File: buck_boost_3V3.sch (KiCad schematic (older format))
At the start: 10 parts

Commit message: Finally finished final draft
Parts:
- C13, C14, C17: renamed from C?; value 10 uF -> 10uF
- C15: renamed from C?; value 10 pF -> 10pF
- C16: renamed from C?; value 3.9 nF -> 3.9nF
- L2: renamed from L?; value 1.5 uH -> 1.5uH
- R4: renamed from R?; value 100 k -> 100k
- R5: renamed from R?; value 562 k -> 562k
- R6: renamed from R?; value 180 k -> 180k
- gave numbers to parts that had none: 1
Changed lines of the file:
@@
 $Descr A4 11693 8268
 encoding utf-8
-Sheet 5 6
+Sheet 4 6
 Title ""
 Date ""
@@
 AR Path="/60C6C1A9" Ref="IC?"  Part="1"
 AR Path="/60BA4931/60C6C1A9" Ref="IC?"  Part="1"
-AR Path="/60BA4931/60C66E04/60C6C1A9" Ref="IC?"  Part="1"
-F 0 "IC?" H 4900 4215 50  0000 C CNN
+AR Path="/60BA4931/60C66E04/60C6C1A9" Ref="IC2"  Part="1"
+F 0 "IC2" H 4900 4215 50  0000 C CNN
 F 1 "TPS63050YFFR" H 4900 4124 50  0000 C CNN
 F 2 "BGA12C40P3X4_129X169X62" H 4450 2900 50  0001 L CNN
@@
 AR Path="/60C6C1B2" Ref="L?"  Part="1"
 AR Path="/60BA4931/60C6C1B2" Ref="L?"  Part="1"
-AR Path="/60BA4931/60C66E04/60C6C1B2" Ref="L?"  Part="1"
-F 0 "L?" V 5090 2750 50  0000 C CNN
-F 1 "1.5 uH" V 4999 2750 50  0000 C CNN
+AR Path="/60BA4931/60C66E04/60C6C1B2" Ref="L2"  Part="1"
+F 0 "L2" V 5090 2750 50  0000 C CNN
+F 1 "1.5uH" V 4999 2750 50  0000 C CNN
 F 2 "" H 4900 2750 50  0001 C CNN
 F 3 "~" H 4900 2750 50  0001 C CNN
@@
 AR Path="/60C6C1C0" Ref="R?"  Part="1"
 AR Path="/60BA4931/60C6C1C0" Ref="R?"  Part="1"
-AR Path="/60BA4931/60C66E04/60C6C1C0" Ref="R?"  Part="1"
-F 0 "R?" H 6068 3596 50  0000 L CNN
-F 1 "562 k" H 6068 3505 50  0000 L CNN
+AR Path="/60BA4931/60C66E04/60C6C1C0" Ref="R5"  Part="1"
+F 0 "R5" H 6068 3596 50  0000 L CNN
+F 1 "562k" H 6068 3505 50  0000 L CNN
 F 2 "" V 6040 3540 50  0001 C CNN
 F 3 "~" H 6000 3550 50  0001 C CNN
@@
 AR Path="/60C6C1CA" Ref="R?"  Part="1"
 AR Path="/60BA4931/60C6C1CA" Ref="R?"  Part="1"
-AR Path="/60BA4931/60C66E04/60C6C1CA" Ref="R?"  Part="1"
-F 0 "R?" H 6068 3996 50  0000 L CNN
-F 1 "180 k" H 6068 3905 50  0000 L CNN
+AR Path="/60BA4931/60C66E04/60C6C1CA" Ref="R6"  Part="1"
+F 0 "R6" H 6068 3996 50  0000 L CNN
+F 1 "180k" H 6068 3905 50  0000 L CNN
 F 2 "" V 6040 3940 50  0001 C CNN
 F 3 "~" H 6000 3950 50  0001 C CNN
@@
 AR Path="/60C6C1DC" Ref="R?"  Part="1"
 AR Path="/60BA4931/60C6C1DC" Ref="R?"  Part="1"
-AR Path="/60BA4931/60C66E04/60C6C1DC" Ref="R?"  Part="1"
-F 0 "R?" H 6968 3846 50  0000 L CNN
-F 1 "100 k" H 6968 3755 50  0000 L CNN
+AR Path="/60BA4931/60C66E04/60C6C1DC" Ref="R4"  Part="1"
+F 0 "R4" H 6968 3846 50  0000 L CNN
+F 1 "100k" H 6968 3755 50  0000 L CNN
 F 2 "" V 6940 3790 50  0001 C CNN
 F 3 "~" H 6900 3800 50  0001 C CNN
@@
 AR Path="/60C6C1E8" Ref="C?"  Part="1"
 AR Path="/60BA4931/60C6C1E8" Ref="C?"  Part="1"
-AR Path="/60BA4931/60C66E04/60C6C1E8" Ref="C?"  Part="1"
-F 0 "C?" H 7415 4196 50  0000 L CNN
-F 1 "10 uF" H 7415 4105 50  0000 L CNN
+AR Path="/60BA4931/60C66E04/60C6C1E8" Ref="C14"  Part="1"
+F 0 "C14" H 7415 4196 50  0000 L CNN
+F 1 "10uF" H 7415 4105 50  0000 L CNN
 F 2 "" H 7338 4000 50  0001 C CNN
 F 3 "~" H 7300 4150 50  0001 C CNN
@@
 AR Path="/60C6C1F2" Ref="C?"  Part="1"
 AR Path="/60BA4931/60C6C1F2" Ref="C?"  Part="1"
-AR Path="/60BA4931/60C66E04/60C6C1F2" Ref="C?"  Part="1"
-F 0 "C?" H 7915 4196 50  0000 L CNN
-F 1 "10 uF" H 7915 4105 50  0000 L CNN
+AR Path="/60BA4931/60C66E04/60C6C1F2" Ref="C13"  Part="1"
+F 0 "C13" H 7915 4196 50  0000 L CNN
+F 1 "10uF" H 7915 4105 50  0000 L CNN
 F 2 "" H 7838 4000 50  0001 C CNN
 F 3 "~" H 7800 4150 50  0001 C CNN
@@
 AR Path="/60C6C210" Ref="C?"  Part="1"
 AR Path="/60BA4931/60C6C210" Ref="C?"  Part="1"
-AR Path="/60BA4931/60C66E04/60C6C210" Ref="C?"  Part="1"
-F 0 "C?" H 4215 4346 50  0000 L CNN
-F 1 "3.9 nF" H 4215 4255 50  0000 L CNN
+AR Path="/60BA4931/60C66E04/60C6C210" Ref="C16"  Part="1"
+F 0 "C16" H 4215 4346 50  0000 L CNN
+F 1 "3.9nF" H 4215 4255 50  0000 L CNN
 F 2 "" H 4138 4150 50  0001 C CNN
 F 3 "~" H 4100 4300 50  0001 C CNN
@@
 AR Path="/60C6C21A" Ref="C?"  Part="1"
 AR Path="/60BA4931/60C6C21A" Ref="C?"  Part="1"
-AR Path="/60BA4931/60C66E04/60C6C21A" Ref="C?"  Part="1"
-F 0 "C?" H 3715 3846 50  0000 L CNN
-F 1 "10 uF" H 3715 3755 50  0000 L CNN
+AR Path="/60BA4931/60C66E04/60C6C21A" Ref="C17"  Part="1"
+F 0 "C17" H 3715 3846 50  0000 L CNN
+F 1 "10uF" H 3715 3755 50  0000 L CNN
 F 2 "" H 3638 3650 50  0001 C CNN
 F 3 "~" H 3600 3800 50  0001 C CNN
@@
 AR Path="/60C6C22B" Ref="C?"  Part="1"
 AR Path="/60BA4931/60C6C22B" Ref="C?"  Part="1"
-AR Path="/60BA4931/60C66E04/60C6C22B" Ref="C?"  Part="1"
-F 0 "C?" H 6615 3996 50  0000 L CNN
-F 1 "10 pF" H 6615 3905 50  0000 L CNN
+AR Path="/60BA4931/60C66E04/60C6C22B" Ref="C15"  Part="1"
+F 0 "C15" H 6615 3996 50  0000 L CNN
+F 1 "10pF" H 6615 3905 50  0000 L CNN
 F 2 "" H 6538 3800 50  0001 C CNN
 F 3 "~" H 6500 3950 50  0001 C CNN

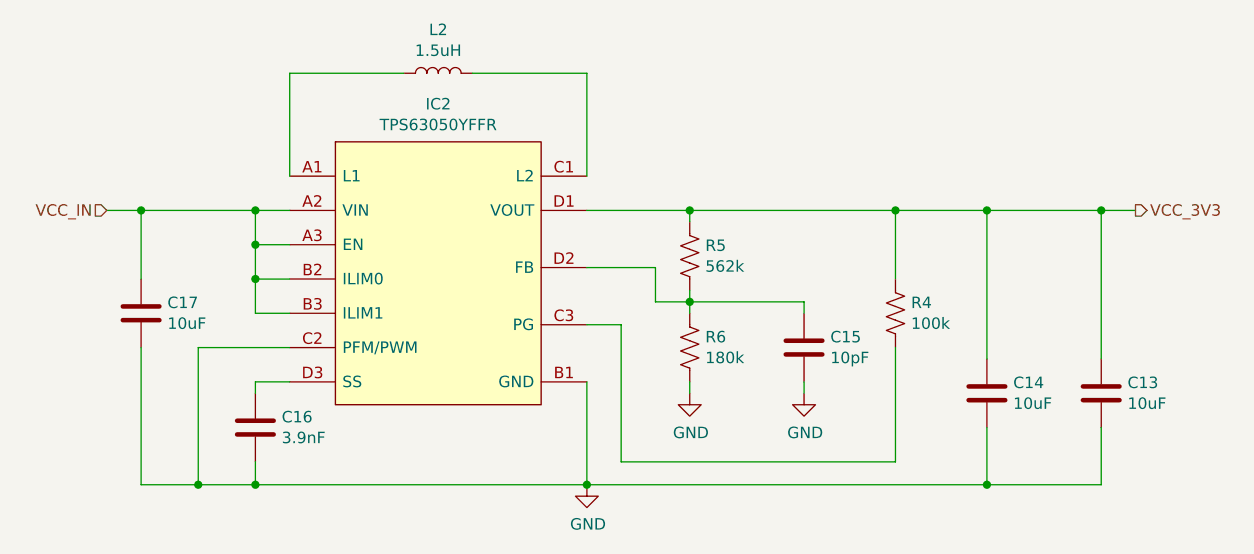
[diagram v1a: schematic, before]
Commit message: Fixed some symbols, assigned some footprints, and made wire labels
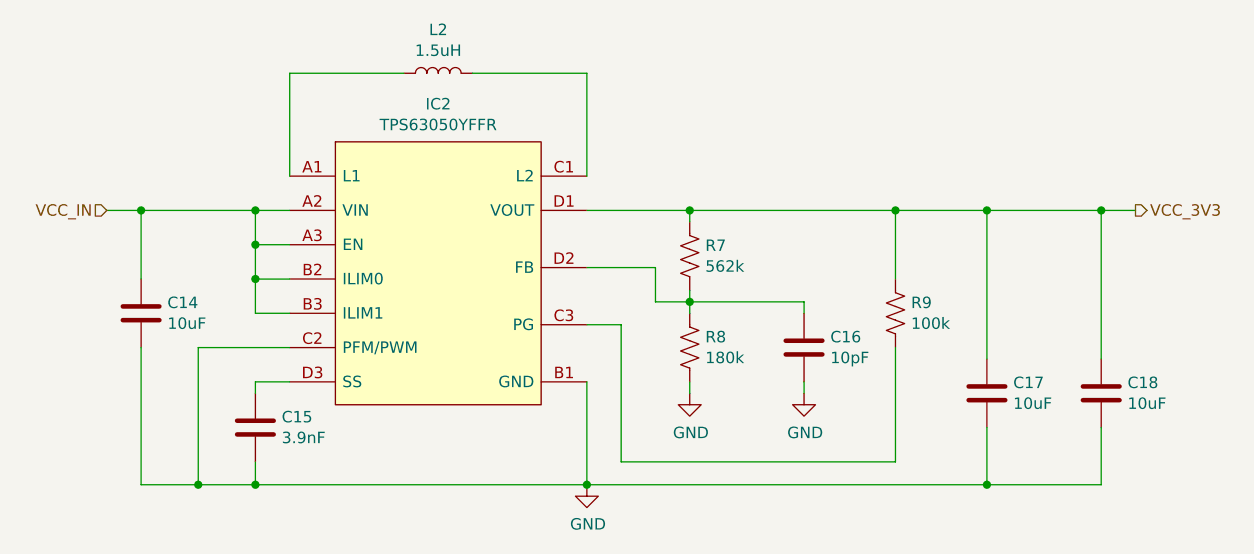
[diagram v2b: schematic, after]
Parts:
- IC2: footprint BGA12C40P3X4_129X169X62 -> Buck_Boost_IC:BGA12C40P3X4_129X169X62
- renumbered C17 to C14, C16 to C15, C15 to C16, C14 to C17, C13 to C18, R5 to R7, R6 to R8, R4 to R9
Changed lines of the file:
@@
 F 0 "IC2" H 4900 4215 50  0000 C CNN
 F 1 "TPS63050YFFR" H 4900 4124 50  0000 C CNN
-F 2 "BGA12C40P3X4_129X169X62" H 4450 2900 50  0001 L CNN
+F 2 "Buck_Boost_IC:BGA12C40P3X4_129X169X62" H 4450 2900 50  0001 L CNN
 F 3 "http://www.ti.com/lit/ds/symlink/tps63050.pdf" H 4450 2800 50  0001 L CNN
 F 4 "TPS6305x Single Inductor Buck-Boost with 1-A Switches and Adjustable Soft Start" H 4450 2700 50  0001 L CNN "Description"
@@
 AR Path="/60C6C1C0" Ref="R?"  Part="1"
 AR Path="/60BA4931/60C6C1C0" Ref="R?"  Part="1"
-AR Path="/60BA4931/60C66E04/60C6C1C0" Ref="R5"  Part="1"
-F 0 "R5" H 6068 3596 50  0000 L CNN
+AR Path="/60BA4931/60C66E04/60C6C1C0" Ref="R7"  Part="1"
+F 0 "R7" H 6068 3596 50  0000 L CNN
 F 1 "562k" H 6068 3505 50  0000 L CNN
 F 2 "" V 6040 3540 50  0001 C CNN
@@
 AR Path="/60C6C1CA" Ref="R?"  Part="1"
 AR Path="/60BA4931/60C6C1CA" Ref="R?"  Part="1"
-AR Path="/60BA4931/60C66E04/60C6C1CA" Ref="R6"  Part="1"
-F 0 "R6" H 6068 3996 50  0000 L CNN
+AR Path="/60BA4931/60C66E04/60C6C1CA" Ref="R8"  Part="1"
+F 0 "R8" H 6068 3996 50  0000 L CNN
 F 1 "180k" H 6068 3905 50  0000 L CNN
 F 2 "" V 6040 3940 50  0001 C CNN
@@
 AR Path="/60C6C1D1" Ref="#PWR?"  Part="1"
 AR Path="/60BA4931/60C6C1D1" Ref="#PWR?"  Part="1"
-AR Path="/60BA4931/60C66E04/60C6C1D1" Ref="#PWR?"  Part="1"
-F 0 "#PWR?" H 6000 3900 50  0001 C CNN
+AR Path="/60BA4931/60C66E04/60C6C1D1" Ref="#PWR020"  Part="1"
+F 0 "#PWR020" H 6000 3900 50  0001 C CNN
 F 1 "GND" H 6005 3977 50  0000 C CNN
 F 2 "" H 6000 4150 50  0001 C CNN
@@
 AR Path="/60C6C1DC" Ref="R?"  Part="1"
 AR Path="/60BA4931/60C6C1DC" Ref="R?"  Part="1"
-AR Path="/60BA4931/60C66E04/60C6C1DC" Ref="R4"  Part="1"
-F 0 "R4" H 6968 3846 50  0000 L CNN
+AR Path="/60BA4931/60C66E04/60C6C1DC" Ref="R9"  Part="1"
+F 0 "R9" H 6968 3846 50  0000 L CNN
 F 1 "100k" H 6968 3755 50  0000 L CNN
 F 2 "" V 6940 3790 50  0001 C CNN
@@
 AR Path="/60C6C1E8" Ref="C?"  Part="1"
 AR Path="/60BA4931/60C6C1E8" Ref="C?"  Part="1"
-AR Path="/60BA4931/60C66E04/60C6C1E8" Ref="C14"  Part="1"
-F 0 "C14" H 7415 4196 50  0000 L CNN
+AR Path="/60BA4931/60C66E04/60C6C1E8" Ref="C17"  Part="1"
+F 0 "C17" H 7415 4196 50  0000 L CNN
 F 1 "10uF" H 7415 4105 50  0000 L CNN
 F 2 "" H 7338 4000 50  0001 C CNN
@@
 AR Path="/60C6C1F2" Ref="C?"  Part="1"
 AR Path="/60BA4931/60C6C1F2" Ref="C?"  Part="1"
-AR Path="/60BA4931/60C66E04/60C6C1F2" Ref="C13"  Part="1"
-F 0 "C13" H 7915 4196 50  0000 L CNN
+AR Path="/60BA4931/60C66E04/60C6C1F2" Ref="C18"  Part="1"
+F 0 "C18" H 7915 4196 50  0000 L CNN
 F 1 "10uF" H 7915 4105 50  0000 L CNN
 F 2 "" H 7838 4000 50  0001 C CNN
@@
 AR Path="/60C6C210" Ref="C?"  Part="1"
 AR Path="/60BA4931/60C6C210" Ref="C?"  Part="1"
-AR Path="/60BA4931/60C66E04/60C6C210" Ref="C16"  Part="1"
-F 0 "C16" H 4215 4346 50  0000 L CNN
+AR Path="/60BA4931/60C66E04/60C6C210" Ref="C15"  Part="1"
+F 0 "C15" H 4215 4346 50  0000 L CNN
 F 1 "3.9nF" H 4215 4255 50  0000 L CNN
 F 2 "" H 4138 4150 50  0001 C CNN
@@
 AR Path="/60C6C21A" Ref="C?"  Part="1"
 AR Path="/60BA4931/60C6C21A" Ref="C?"  Part="1"
-AR Path="/60BA4931/60C66E04/60C6C21A" Ref="C17"  Part="1"
-F 0 "C17" H 3715 3846 50  0000 L CNN
+AR Path="/60BA4931/60C66E04/60C6C21A" Ref="C14"  Part="1"
+F 0 "C14" H 3715 3846 50  0000 L CNN
 F 1 "10uF" H 3715 3755 50  0000 L CNN
 F 2 "" H 3638 3650 50  0001 C CNN
@@
 AR Path="/60C6C225" Ref="#PWR?"  Part="1"
 AR Path="/60BA4931/60C6C225" Ref="#PWR?"  Part="1"
-AR Path="/60BA4931/60C66E04/60C6C225" Ref="#PWR?"  Part="1"
-F 0 "#PWR?" H 6500 3900 50  0001 C CNN
+AR Path="/60BA4931/60C66E04/60C6C225" Ref="#PWR021"  Part="1"
+F 0 "#PWR021" H 6500 3900 50  0001 C CNN
 F 1 "GND" H 6505 3977 50  0000 C CNN
 F 2 "" H 6500 4150 50  0001 C CNN
@@
 AR Path="/60C6C22B" Ref="C?"  Part="1"
 AR Path="/60BA4931/60C6C22B" Ref="C?"  Part="1"
-AR Path="/60BA4931/60C66E04/60C6C22B" Ref="C15"  Part="1"
-F 0 "C15" H 6615 3996 50  0000 L CNN
+AR Path="/60BA4931/60C66E04/60C6C22B" Ref="C16"  Part="1"
+F 0 "C16" H 6615 3996 50  0000 L CNN
 F 1 "10pF" H 6615 3905 50  0000 L CNN
 F 2 "" H 6538 3800 50  0001 C CNN
@@
 AR Path="/60C6C232" Ref="#PWR?"  Part="1"
 AR Path="/60BA4931/60C6C232" Ref="#PWR?"  Part="1"
-AR Path="/60BA4931/60C66E04/60C6C232" Ref="#PWR?"  Part="1"
-F 0 "#PWR?" H 5550 4300 50  0001 C CNN
+AR Path="/60BA4931/60C66E04/60C6C232" Ref="#PWR019"  Part="1"
+F 0 "#PWR019" H 5550 4300 50  0001 C CNN
 F 1 "GND" H 5555 4377 50  0000 C CNN
 F 2 "" H 5550 4550 50  0001 C CNN

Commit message: Chose more parts and added more footprints. Have some resistors and all the capacitors to go
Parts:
- removed L2: 1.5uH, symbol Device:L
- added L2: DFE252012P-1R5M=P2, Inductor_SMD:DFE2HCAH1R0MJ0L, symbol Inductor_1v5uH:DFE252012P-1R5M=P2
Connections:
- net at IC2.A1 (L1): now also L2.1
- net at IC2.C1 (L2): now also L2.2
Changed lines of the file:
@@
 Wire Wire Line
 	5550 2750 5550 3200
-$Comp
-L Device:L L?
-U 1 1 60C6C1B2
-P 4900 2750
-AR Path="/60C6C1B2" Ref="L?"  Part="1"
-AR Path="/60BA4931/60C6C1B2" Ref="L?"  Part="1"
-AR Path="/60BA4931/60C66E04/60C6C1B2" Ref="L2"  Part="1"
-F 0 "L2" V 5090 2750 50  0000 C CNN
-F 1 "1.5uH" V 4999 2750 50  0000 C CNN
-F 2 "" H 4900 2750 50  0001 C CNN
-F 3 "~" H 4900 2750 50  0001 C CNN
-	1    4900 2750
-	0    -1   -1   0
-$EndComp
 Wire Wire Line
 	5050 2750 5550 2750
@@
 Text HLabel 3450 3350 0    50   Input ~ 0
 VCC_IN
+$Comp
+L Inductor_1v5uH:DFE252012P-1R5M=P2 L2
+U 1 1 607620B4
+P 4900 2750
+F 0 "L2" H 4900 2940 50  0000 C CNN
+F 1 "DFE252012P-1R5M=P2" H 4900 2849 50  0000 C CNN
+F 2 "Inductor_SMD:DFE2HCAH1R0MJ0L" H 4550 2550 50  0001 L CNN
+F 3 "https://psearch.en.murata.com/inductor/product/DFE252012P-1R5M%23.html" H 4550 2450 50  0001 L CNN
+F 4 "Toko DFE252012P Series Shielded Wire-wound SMD Inductor with a Powered Iron Core, 1.5 uH Wire-Wound 3.9A Idc" H 4550 2350 50  0001 L CNN "Description"
+F 5 "1.2" H 4550 2250 50  0001 L CNN "Height"
+F 6 "Murata Electronics" H 4550 2150 50  0001 L CNN "Manufacturer_Name"
+F 7 "DFE252012P-1R5M=P2" H 4550 2050 50  0001 L CNN "Manufacturer_Part_Number"
+F 8 "81-DFE252012P-1R5MP2" H 4550 1950 50  0001 L CNN "Mouser Part Number"
+F 9 "https://www.mouser.co.uk/ProductDetail/Murata-Electronics/DFE252012P-1R5M%3dP2?qs=KuGPmAKtFKVOutr53B1A3A%3D%3D" H 4550 1850 50  0001 L CNN "Mouser Price/Stock"
+F 10 "DFE252012P-1R5M=P2" H 4550 1750 50  0001 L CNN "Arrow Part Number"
+F 11 "https://www.arrow.com/en/products/dfe252012p-1r5mp2/murata-manufacturing" H 4550 1650 50  0001 L CNN "Arrow Price/Stock"
+	1    4900 2750
+	1    0    0    -1
+$EndComp
 $EndSCHEMATC

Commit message: Finished assigning footprints, and generated netlist
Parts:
- C14, C17, C18: footprint (none) -> Capacitor_SMD:C_0805_2012Metric
- C15: value 3.9nF -> 4.7nF; footprint (none) -> Capacitor_SMD:C_0603_1608Metric
- C16: footprint (none) -> Capacitor_SMD:C_0603_1608Metric
- R7, R9: footprint (none) -> Resistor_SMD:R_0603_1608Metric
- R8: footprint (none) -> Resistor_SMD:R_1206_3216Metric
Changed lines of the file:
@@
 F 0 "R7" H 6068 3596 50  0000 L CNN
 F 1 "562k" H 6068 3505 50  0000 L CNN
-F 2 "" V 6040 3540 50  0001 C CNN
+F 2 "Resistor_SMD:R_0603_1608Metric" V 6040 3540 50  0001 C CNN
 F 3 "~" H 6000 3550 50  0001 C CNN
 	1    6000 3550
@@
 F 0 "R8" H 6068 3996 50  0000 L CNN
 F 1 "180k" H 6068 3905 50  0000 L CNN
-F 2 "" V 6040 3940 50  0001 C CNN
+F 2 "Resistor_SMD:R_1206_3216Metric" V 6040 3940 50  0001 C CNN
 F 3 "~" H 6000 3950 50  0001 C CNN
 	1    6000 3950
@@
 F 0 "R9" H 6968 3846 50  0000 L CNN
 F 1 "100k" H 6968 3755 50  0000 L CNN
-F 2 "" V 6940 3790 50  0001 C CNN
+F 2 "Resistor_SMD:R_0603_1608Metric" V 6940 3790 50  0001 C CNN
 F 3 "~" H 6900 3800 50  0001 C CNN
 	1    6900 3800
@@
 F 0 "C17" H 7415 4196 50  0000 L CNN
 F 1 "10uF" H 7415 4105 50  0000 L CNN
-F 2 "" H 7338 4000 50  0001 C CNN
+F 2 "Capacitor_SMD:C_0805_2012Metric" H 7338 4000 50  0001 C CNN
 F 3 "~" H 7300 4150 50  0001 C CNN
 	1    7300 4150
@@
 F 0 "C18" H 7915 4196 50  0000 L CNN
 F 1 "10uF" H 7915 4105 50  0000 L CNN
-F 2 "" H 7838 4000 50  0001 C CNN
+F 2 "Capacitor_SMD:C_0805_2012Metric" H 7838 4000 50  0001 C CNN
 F 3 "~" H 7800 4150 50  0001 C CNN
 	1    7800 4150
@@
 AR Path="/60BA4931/60C66E04/60C6C210" Ref="C15"  Part="1"
 F 0 "C15" H 4215 4346 50  0000 L CNN
-F 1 "3.9nF" H 4215 4255 50  0000 L CNN
-F 2 "" H 4138 4150 50  0001 C CNN
+F 1 "4.7nF" H 4215 4255 50  0000 L CNN
+F 2 "Capacitor_SMD:C_0603_1608Metric" H 4138 4150 50  0001 C CNN
 F 3 "~" H 4100 4300 50  0001 C CNN
 	1    4100 4300
@@
 F 0 "C14" H 3715 3846 50  0000 L CNN
 F 1 "10uF" H 3715 3755 50  0000 L CNN
-F 2 "" H 3638 3650 50  0001 C CNN
+F 2 "Capacitor_SMD:C_0805_2012Metric" H 3638 3650 50  0001 C CNN
 F 3 "~" H 3600 3800 50  0001 C CNN
 	1    3600 3800
@@
 F 0 "C16" H 6615 3996 50  0000 L CNN
 F 1 "10pF" H 6615 3905 50  0000 L CNN
-F 2 "" H 6538 3800 50  0001 C CNN
+F 2 "Capacitor_SMD:C_0603_1608Metric" H 6538 3800 50  0001 C CNN
 F 3 "~" H 6500 3950 50  0001 C CNN
 	1    6500 3950
